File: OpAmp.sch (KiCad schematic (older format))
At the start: 47 parts, among them J1 Conn_01x05, J2 Conn_01x02, J3 Conn_01x02, J4 Conn_01x02, Q1 5551, Q10 5401, Q11 5551, Q12 5551, Q13 5551, Q14 5401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

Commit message: JLCPCB order 2021-04-11
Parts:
- removed C5: 100 nF, Capacitors_SMD:C_0805_HandSoldering, symbol C
- removed D1, D2: D_x2_Serial_AKC, TO_SOT_Packages_SMD:SOT-23, symbol D_x2_Serial_AKC
- removed Q3, Q6: 5551, TO_SOT_Packages_SMD:SOT-23, symbol MMBT3904
- added R14, R15: 680R, Resistors_SMD:R_0805_HandSoldering, symbol R
- R2: value 330R -> 680R; LCSC C17630 -> C17798
- RV1: value 1k -> 2k
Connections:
- net at C7.1, Q2.3 (C), Q8.1 (B): now also Q1.3 (C)
- net at Q1.2 (E), RV1.3: now also R14.2
- net at Q7.2 (E), RV1.1: now also R15.1
- net at Q7.3 (C): now also Q2.1 (B), Q5.1 (B), Q5.3 (C)
- net at Q4.3 (C), RV1.2: now also R14.1, R15.2
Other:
- moved on the sheet: C1, C2, C3, C4, Q1, Q7, RV1

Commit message: Added partial outputs
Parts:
- removed J1: Conn_01x05, Pin_Headers:Pin_Header_Straight_1x05_Pitch2.54mm, symbol Conn_01x05
- removed J4: Conn_01x02, Pin_Headers:Pin_Header_Straight_1x02_Pitch2.54mm, symbol Conn_01x02
- added J1: Conn_01x07, Pin_Headers:Pin_Header_Straight_1x07_Pitch2.54mm, symbol Conn_01x07
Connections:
- net NEG: now also J1.3 (Pin_3)
- net OUT: now also J1.4 (Pin_4)
- net POS: now also J1.2 (Pin_2)
- net VCC: now also J1.5 (Pin_5)
- net VEE: now also J1.1 (Pin_1)
- net DRVPLUS: now reaches Q15.2 (E), R12.1
- net DRVPLUS: now also J1.7 (Pin_7)
- net DRVMINUS: now reaches Q16.2 (E), R13.2
- net DRVMINUS: now also J1.6 (Pin_6)
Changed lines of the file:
@@
 $EndComp
 $Comp
-L VCC #PWR2
+L VCC #PWR01
 U 1 1 6064E2D7
-P 1000 4300
-F 0 "#PWR2" H 1000 4150 50  0001 C CNN
-F 1 "VCC" H 1000 4450 50  0000 C CNN
-F 2 "" H 1000 4300 50  0001 C CNN
-F 3 "" H 1000 4300 50  0001 C CNN
-	1    1000 4300
-	1    0    0    -1
-$EndComp
-$Comp
-L VEE #PWR1
+P 1050 4300
+F 0 "#PWR01" H 1050 4150 50  0001 C CNN
+F 1 "VCC" H 1050 4450 50  0000 C CNN
+F 2 "" H 1050 4300 50  0001 C CNN
+F 3 "" H 1050 4300 50  0001 C CNN
+	1    1050 4300
+	1    0    0    -1
+$EndComp
+$Comp
+L VEE #PWR02
 U 1 1 6064E2F5
-P 1000 3900
-F 0 "#PWR1" H 1000 3750 50  0001 C CNN
-F 1 "VEE" H 1000 4050 50  0000 C CNN
-F 2 "" H 1000 3900 50  0001 C CNN
-F 3 "" H 1000 3900 50  0001 C CNN
-	1    1000 3900
+P 1050 3900
+F 0 "#PWR02" H 1050 3750 50  0001 C CNN
+F 1 "VEE" H 1050 4050 50  0000 C CNN
+F 2 "" H 1050 3900 50  0001 C CNN
+F 3 "" H 1050 3900 50  0001 C CNN
+	1    1050 3900
 	-1   0    0    1
 $EndComp
@@
 Text Label 3800 3000 0    60   ~ 0
 NEG
-$Comp
-L Conn_01x05 J1
-U 1 1 6064E380
-P 1650 4100
-F 0 "J1" H 1650 4400 50  0000 C CNN
-F 1 "Conn_01x05" H 1650 3800 50  0000 C CNN
-F 2 "Pin_Headers:Pin_Header_Straight_1x05_Pitch2.54mm" H 1650 4100 50  0001 C CNN
-F 3 "" H 1650 4100 50  0001 C CNN
-	1    1650 4100
-	1    0    0    -1
-$EndComp
 Text Label 1300 4200 2    60   ~ 0
 OUT
@@
 $EndComp
 $Comp
-L VCC #PWR6
+L VCC #PWR03
 U 1 1 6064EEAE
 P 2800 750
-F 0 "#PWR6" H 2800 600 50  0001 C CNN
+F 0 "#PWR03" H 2800 600 50  0001 C CNN
 F 1 "VCC" H 2800 900 50  0000 C CNN
 F 2 "" H 2800 750 50  0001 C CNN
@@
 $EndComp
 $Comp
-L VEE #PWR7
+L VEE #PWR04
 U 1 1 6064F415
 P 2850 5100
-F 0 "#PWR7" H 2850 4950 50  0001 C CNN
+F 0 "#PWR04" H 2850 4950 50  0001 C CNN
 F 1 "VEE" H 2850 5250 50  0000 C CNN
 F 2 "" H 2850 5100 50  0001 C CNN
@@
 $EndComp
 $Comp
-L VCC #PWR9
+L VCC #PWR05
 U 1 1 6065149D
 P 4500 3200
-F 0 "#PWR9" H 4500 3050 50  0001 C CNN
+F 0 "#PWR05" H 4500 3050 50  0001 C CNN
 F 1 "VCC" H 4500 3350 50  0000 C CNN
 F 2 "" H 4500 3200 50  0001 C CNN
@@
 $EndComp
 $Comp
-L VEE #PWR8
+L VEE #PWR06
 U 1 1 606515F7
 P 4300 2850
-F 0 "#PWR8" H 4300 2700 50  0001 C CNN
+F 0 "#PWR06" H 4300 2700 50  0001 C CNN
 F 1 "VEE" H 4300 3000 50  0000 C CNN
 F 2 "" H 4300 2850 50  0001 C CNN
@@
 $EndComp
 $Comp
-L VEE #PWR5
+L VEE #PWR07
 U 1 1 60654F68
 P 1750 2550
-F 0 "#PWR5" H 1750 2400 50  0001 C CNN
+F 0 "#PWR07" H 1750 2400 50  0001 C CNN
 F 1 "VEE" H 1750 2700 50  0000 C CNN
 F 2 "" H 1750 2550 50  0001 C CNN
@@
 $EndComp
 $Comp
-L VEE #PWR3
+L VEE #PWR08
 U 1 1 60657BCF
 P 1250 4800
-F 0 "#PWR3" H 1250 4650 50  0001 C CNN
+F 0 "#PWR08" H 1250 4650 50  0001 C CNN
 F 1 "VEE" H 1250 4950 50  0000 C CNN
 F 2 "" H 1250 4800 50  0001 C CNN
@@
 $EndComp
 $Comp
-L VCC #PWR4
+L VCC #PWR09
 U 1 1 60657EDE
 P 1250 5200
-F 0 "#PWR4" H 1250 5050 50  0001 C CNN
+F 0 "#PWR09" H 1250 5050 50  0001 C CNN
 F 1 "VCC" H 1250 5350 50  0000 C CNN
 F 2 "" H 1250 5200 50  0001 C CNN
@@
 Text Notes 7650 6850 0    60   ~ 0
 Discrete Op-Amp by DLM\nCC-BY-SA 4.0
-$Comp
-L Conn_01x02 J4
-U 1 1 6065938E
-P 7850 3200
-F 0 "J4" H 7850 3300 50  0000 C CNN
-F 1 "Conn_01x02" H 7850 3000 50  0000 C CNN
-F 2 "Pin_Headers:Pin_Header_Straight_1x02_Pitch2.54mm" H 7850 3200 50  0001 C CNN
-F 3 "" H 7850 3200 50  0001 C CNN
-	1    7850 3200
-	1    0    0    -1
-$EndComp
 Wire Wire Line
 	2100 3000 1750 3000
@@
 	3800 3000 3550 3000
 Wire Wire Line
-	1000 3900 1450 3900
-Wire Wire Line
-	1000 4300 1450 4300
+	1050 3900 1450 3900
+Wire Wire Line
+	1050 4300 1450 4300
 Wire Wire Line
 	1300 4200 1450 4200
@@
 Connection ~ 3900 2300
 Wire Wire Line
-	7300 2650 7300 2550
+	7300 2550 7300 2650
 Wire Wire Line
 	7300 2950 7300 3100
@@
 Connection ~ 6450 3700
 Wire Wire Line
-	7300 3500 7300 3400
+	7300 3400 7300 3500
 Wire Wire Line
 	7300 5050 7300 3900
@@
 Wire Wire Line
 	1450 5200 1450 5300
-Wire Wire Line
-	7650 3300 7650 3450
-Wire Wire Line
-	7650 3450 7300 3450
 Connection ~ 7300 3450
-Wire Wire Line
-	7450 3000 7450 3200
-Wire Wire Line
-	7450 3200 7650 3200
 Wire Wire Line
 	7300 3000 7500 3000
@@
 	0    1    1    0
 $EndComp
-Connection ~ 7450 3000
+Text Label 7500 2600 0    60   ~ 0
+DRVPLUS
+Wire Wire Line
+	7500 2600 7300 2600
+Connection ~ 7300 2600
+Text Label 7500 3450 0    60   ~ 0
+DRVMINUS
+Wire Wire Line
+	7300 3450 7500 3450
+$Comp
+L Conn_01x07 J1
+U 1 1 60A20C90
+P 1650 4200
+F 0 "J1" H 1650 4600 50  0000 C CNN
+F 1 "Conn_01x07" H 1650 3800 50  0000 C CNN
+F 2 "Pin_Headers:Pin_Header_Straight_1x07_Pitch2.54mm" H 1650 4200 50  0001 C CNN
+F 3 "" H 1650 4200 50  0001 C CNN
+	1    1650 4200
+	1    0    0    -1
+$EndComp
+Text Label 950  4500 2    60   ~ 0
+DRVPLUS
+Wire Wire Line
+	1450 4500 950  4500
+Text Label 950  4400 2    60   ~ 0
+DRVMINUS
+Wire Wire Line
+	950  4400 1450 4400
 $EndSCHEMATC

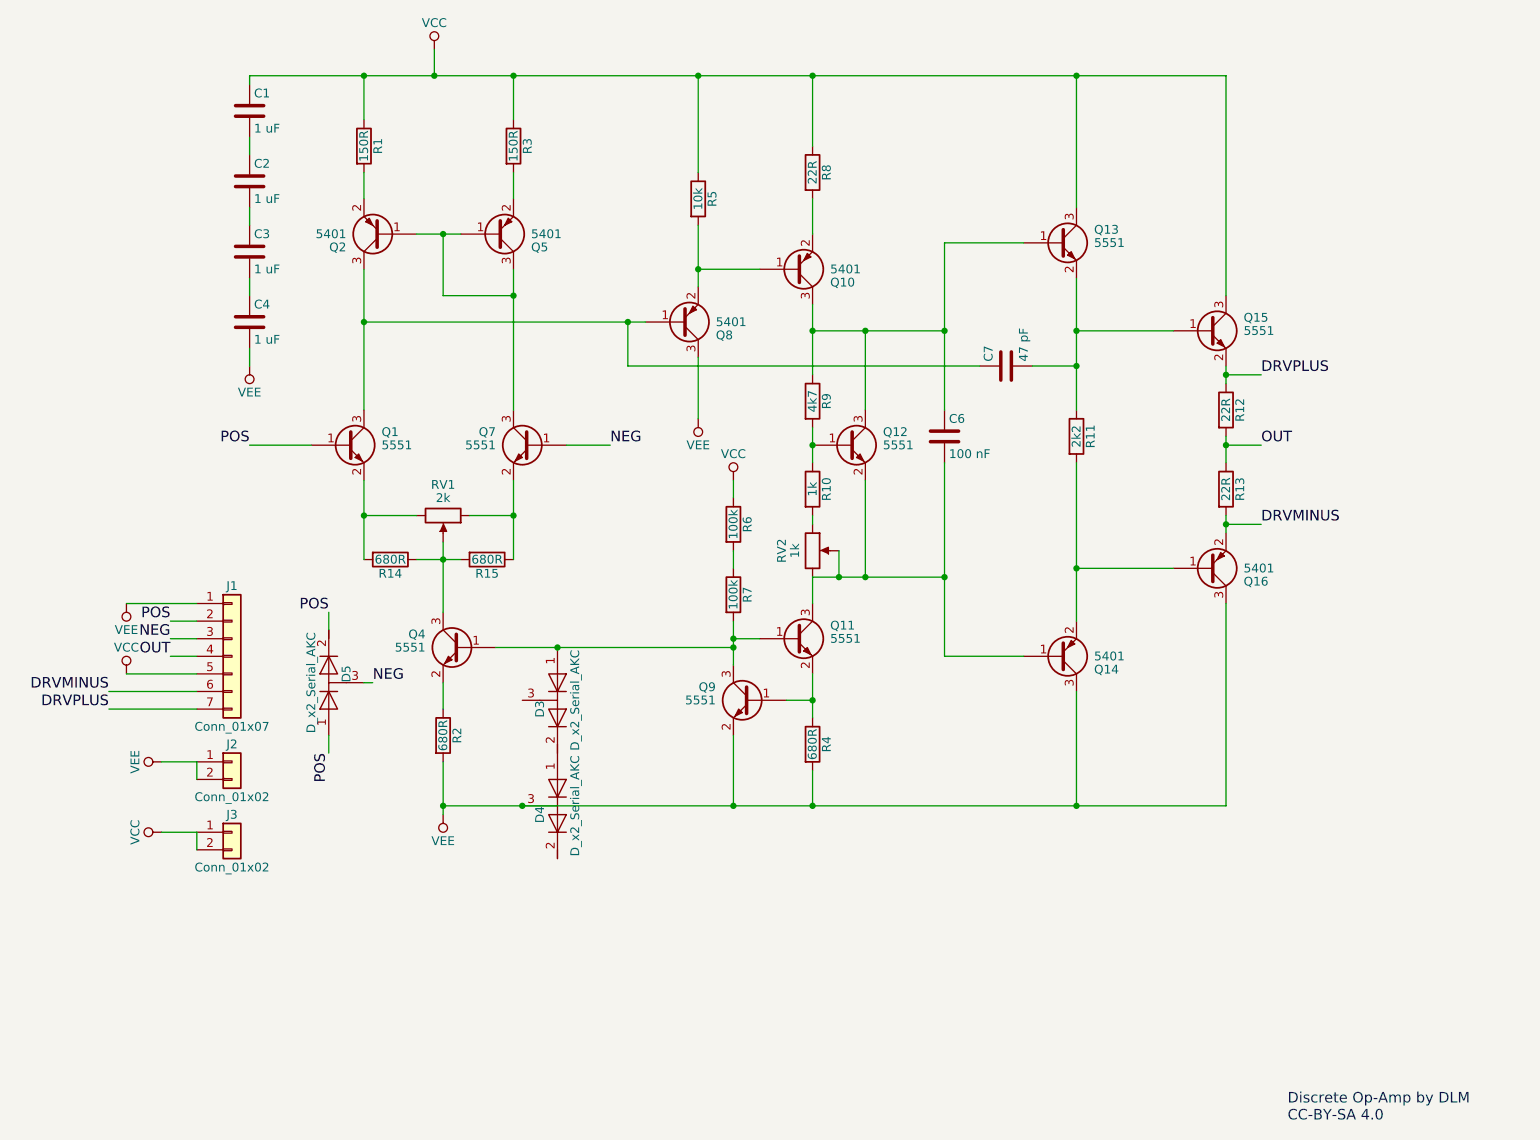
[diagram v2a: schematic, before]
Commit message: Add spot for power transistors
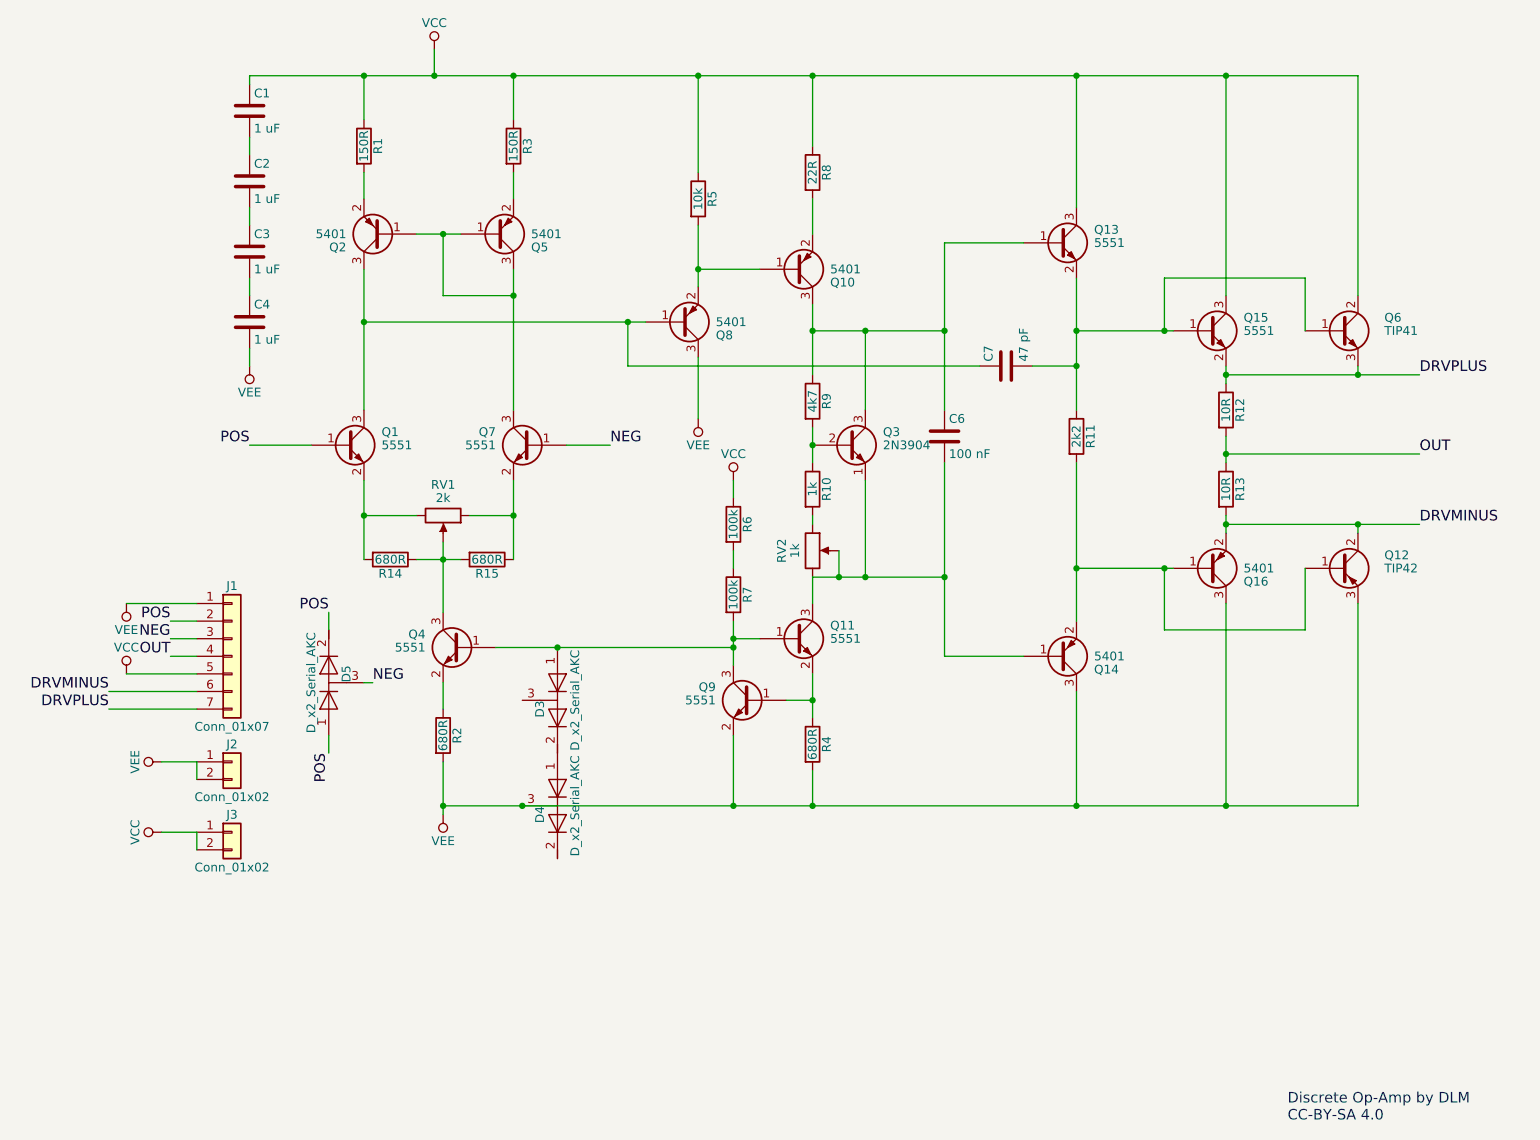
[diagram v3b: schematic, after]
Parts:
- removed Q12: 5551, TO_SOT_Packages_SMD:SOT-23, symbol MMBT3904
- added Q12: TIP42, TO_SOT_Packages_THT:TO-220-3_Vertical, symbol TIP42
- added Q3: 2N3904, TO_SOT_Packages_THT:TO-92_Inline_Wide, symbol 2N3904
- added Q6: TIP41, TO_SOT_Packages_THT:TO-220-3_Vertical, symbol TIP41
- R12, R13: value 22R -> 10R; footprint Resistors_SMD:R_0805_HandSoldering -> Resistors_SMD:R_1206_HandSoldering; LCSC C17561 -> C17903
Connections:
- net DRVMINUS: now also Q12.2 (C)
- net DRVPLUS: now also Q6.3 (E)
- net VCC: now also Q6.2 (C)
- net VEE: now also Q12.3 (E)
- net at C6.1, Q10.3 (C), Q13.1 (B)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: now also Q3.3 (C)
- net at C6.2, Q11.3 (C), Q14.1 (B)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: now also Q3.1 (E)
- net at R10.1, R9.2: now also Q3.2 (B)
- net at C7.2, Q13.2 (E), Q15.1 (B)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: now also Q6.1 (B)
- net at Q14.2 (E), Q16.1 (B), R11.2: now also Q12.1 (B)
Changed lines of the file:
@@
-$EndComp
-$Comp
-L MMBT3904 Q12
-U 1 1 60651A38
-P 5150 3000
-F 0 "Q12" H 5350 3075 50  0000 L CNN
-F 1 "5551" H 5350 3000 50  0000 L CNN
-F 2 "TO_SOT_Packages_SMD:SOT-23" H 5350 2925 50  0001 L CIN
-F 3 "" H 5150 3000 50  0001 L CNN
-F 4 "C2145" H 5150 3000 60  0001 C CNN "LCSC"
-	1    5150 3000
-	1    0    0    -1
 $EndComp
 $Comp
@@
 P 7300 2800
 F 0 "R12" V 7380 2800 50  0000 C CNN
-F 1 "22R" V 7300 2800 50  0000 C CNN
-F 2 "Resistors_SMD:R_0805_HandSoldering" V 7230 2800 50  0001 C CNN
+F 1 "10R" V 7300 2800 50  0000 C CNN
+F 2 "Resistors_SMD:R_1206_HandSoldering" V 7230 2800 50  0001 C CNN
 F 3 "" H 7300 2800 50  0001 C CNN
-F 4 " C17561" V 7300 2800 60  0001 C CNN "LCSC"
+F 4 "C17903" V 7300 2800 60  0001 C CNN "LCSC"
 	1    7300 2800
 	1    0    0    -1
@@
 P 7300 3250
 F 0 "R13" V 7380 3250 50  0000 C CNN
-F 1 "22R" V 7300 3250 50  0000 C CNN
-F 2 "Resistors_SMD:R_0805_HandSoldering" V 7230 3250 50  0001 C CNN
+F 1 "10R" V 7300 3250 50  0000 C CNN
+F 2 "Resistors_SMD:R_1206_HandSoldering" V 7230 3250 50  0001 C CNN
 F 3 "" H 7300 3250 50  0001 C CNN
-F 4 " C17561" V 7300 3250 60  0001 C CNN "LCSC"
+F 4 "C17903" V 7300 3250 60  0001 C CNN "LCSC"
 	1    7300 3250
 	1    0    0    -1
 $EndComp
-Text Label 7500 3000 0    60   ~ 0
+Text Label 8400 3050 0    60   ~ 0
 OUT
 $Comp
@@
 	4500 4150 3150 4150
 Wire Wire Line
-	2850 5050 7300 5050
+	2850 5050 8050 5050
 Connection ~ 2850 5050
 Wire Wire Line
 	2400 1150 2400 900
 Wire Wire Line
-	1750 900  7300 900
+	1750 900  8050 900
 Wire Wire Line
 	3250 900  3250 1150
@@
 Connection ~ 6450 900
 Wire Wire Line
-	7000 2350 6450 2350
+	6450 2350 7000 2350
 Connection ~ 6450 2350
 Wire Wire Line
@@
 Connection ~ 5700 3750
 Wire Wire Line
-	7000 3700 6450 3700
+	6450 3700 7000 3700
 Connection ~ 6450 3700
 Wire Wire Line
@@
 	7300 5050 7300 3900
 Connection ~ 6450 5050
-Connection ~ 7300 3000
 Wire Wire Line
 	1750 2150 1750 2050
@@
 Wire Wire Line
 	1450 5200 1450 5300
-Connection ~ 7300 3450
-Wire Wire Line
-	7300 3000 7500 3000
 Wire Wire Line
 	1750 900  1750 950
@@
 	0    1    1    0
 $EndComp
-Text Label 7500 2600 0    60   ~ 0
+Text Label 8400 2600 0    60   ~ 0
 DRVPLUS
-Wire Wire Line
-	7500 2600 7300 2600
-Connection ~ 7300 2600
-Text Label 7500 3450 0    60   ~ 0
+Text Label 8400 3450 0    60   ~ 0
 DRVMINUS
-Wire Wire Line
-	7300 3450 7500 3450
 $Comp
 L Conn_01x07 J1
@@
 Wire Wire Line
 	950  4400 1450 4400
+$Comp
+L 2N3904 Q3
+U 1 1 60A57D41
+P 5150 3000
+F 0 "Q3" H 5350 3075 50  0000 L CNN
+F 1 "2N3904" H 5350 3000 50  0000 L CNN
+F 2 "TO_SOT_Packages_THT:TO-92_Inline_Wide" H 5350 2925 50  0001 L CIN
+F 3 "" H 5150 3000 50  0001 L CNN
+	1    5150 3000
+	1    0    0    -1
+$EndComp
+$Comp
+L TIP41 Q6
+U 1 1 60A580E8
+P 7950 2350
+F 0 "Q6" H 8200 2425 50  0000 L CNN
+F 1 "TIP41" H 8200 2350 50  0000 L CNN
+F 2 "TO_SOT_Packages_THT:TO-220-3_Vertical" H 8200 2275 50  0001 L CIN
+F 3 "" H 7950 2350 50  0001 L CNN
+	1    7950 2350
+	1    0    0    -1
+$EndComp
+$Comp
+L TIP42 Q12
+U 1 1 60A5818E
+P 7950 3700
+F 0 "Q12" H 8200 3775 50  0000 L CNN
+F 1 "TIP42" H 8200 3700 50  0000 L CNN
+F 2 "TO_SOT_Packages_THT:TO-220-3_Vertical" H 8200 3625 50  0001 L CIN
+F 3 "" H 7950 3700 50  0001 L CNN
+	1    7950 3700
+	1    0    0    -1
+$EndComp
+Wire Wire Line
+	6950 2350 6950 2050
+Wire Wire Line
+	6950 2050 7750 2050
+Wire Wire Line
+	7750 2050 7750 2350
+Connection ~ 6950 2350
+Wire Wire Line
+	7750 4050 7750 3700
+Wire Wire Line
+	6950 4050 7750 4050
+Wire Wire Line
+	8050 5050 8050 3900
+Connection ~ 7300 5050
+Wire Wire Line
+	8050 900  8050 2150
+Connection ~ 7300 900
+Wire Wire Line
+	7300 2600 8400 2600
+Connection ~ 7300 2600
+Wire Wire Line
+	8050 2550 8050 2600
+Connection ~ 8050 2600
+Wire Wire Line
+	8050 3500 8050 3450
+Wire Wire Line
+	7300 3450 8400 3450
+Connection ~ 7300 3450
+Connection ~ 8050 3450
+Wire Wire Line
+	8400 3050 7300 3050
+Connection ~ 7300 3050
+Wire Wire Line
+	6950 4050 6950 3700
+Connection ~ 6950 3700
 $EndSCHEMATC

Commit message: JLCPCB manufacturing
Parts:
- R12, R13: value 10R -> 22R; LCSC C17903 -> C17958
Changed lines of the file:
@@
 P 7300 2800
 F 0 "R12" V 7380 2800 50  0000 C CNN
-F 1 "10R" V 7300 2800 50  0000 C CNN
+F 1 "22R" V 7300 2800 50  0000 C CNN
 F 2 "Resistors_SMD:R_1206_HandSoldering" V 7230 2800 50  0001 C CNN
 F 3 "" H 7300 2800 50  0001 C CNN
-F 4 "C17903" V 7300 2800 60  0001 C CNN "LCSC"
+F 4 "C17958" V 7300 2800 60  0001 C CNN "LCSC"
 	1    7300 2800
 	1    0    0    -1
@@
 P 7300 3250
 F 0 "R13" V 7380 3250 50  0000 C CNN
-F 1 "10R" V 7300 3250 50  0000 C CNN
+F 1 "22R" V 7300 3250 50  0000 C CNN
 F 2 "Resistors_SMD:R_1206_HandSoldering" V 7230 3250 50  0001 C CNN
 F 3 "" H 7300 3250 50  0001 C CNN
-F 4 "C17903" V 7300 3250 60  0001 C CNN "LCSC"
+F 4 "C17958" V 7300 3250 60  0001 C CNN "LCSC"
 	1    7300 3250
 	1    0    0    -1
